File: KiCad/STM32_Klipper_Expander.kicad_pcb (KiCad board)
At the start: 2 copper layers, 48.3 x 48.3 mm, 44 parts, among them J1 USB_B_Micro, J10 Conn_01x01, J11 Conn_01x03, J12 Conn_01x02, J2 Conn_01x04, J3 Conn_02x05, J4 Conn_01x03, J5 Vin, J6 Screw_Terminal_01x08, J7 Conn_01x02, J8 Conn_01x02, J9 Conn_01x02, Q1 IRLML6344TRPBF, Q2 IRLML6344TRPBF, Q3 IRLML6344TRPBF, Q4 IRLML6344TRPBF, SW2 SW_SPST, U1 STM32F042F6Px, U2 AP2127K-3.3, U3 74LVC1G17

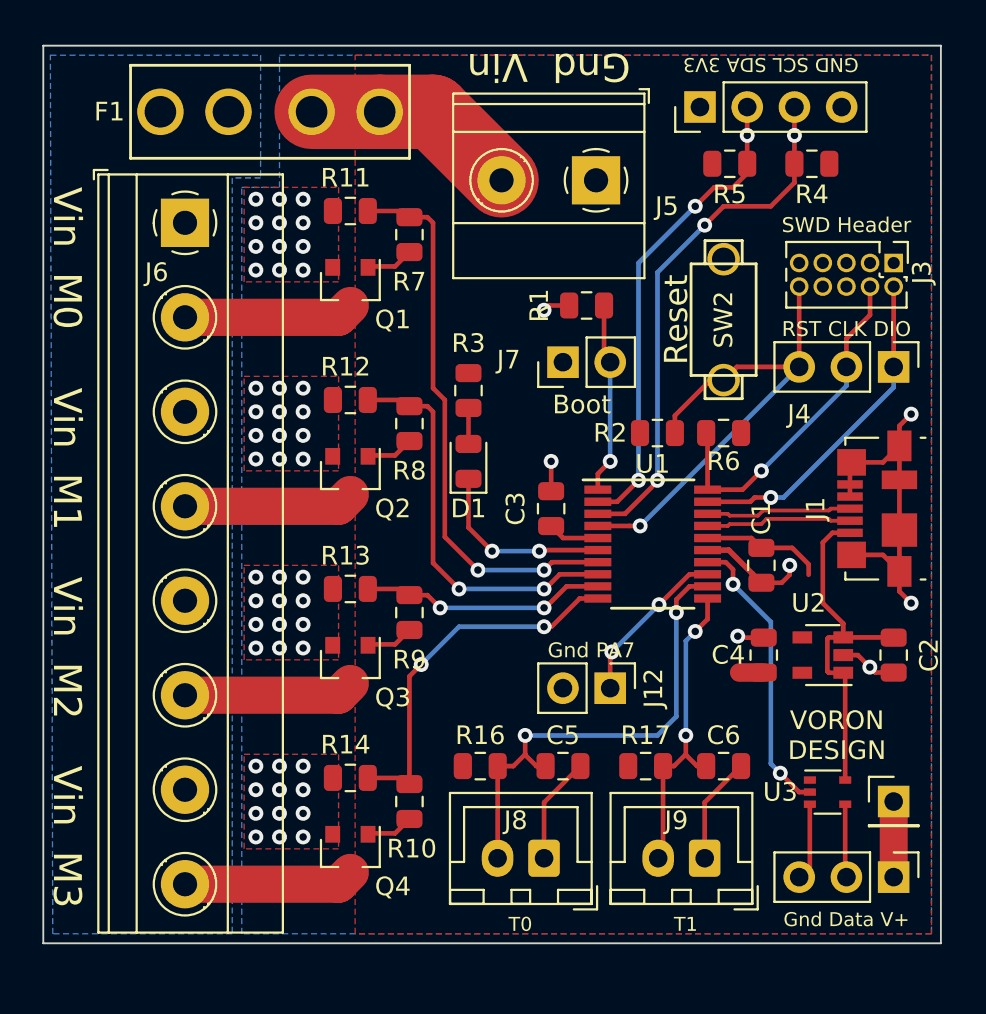
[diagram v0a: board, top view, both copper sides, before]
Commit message: Addition of mounting hole
APPARENTLY we need some way to mount this....
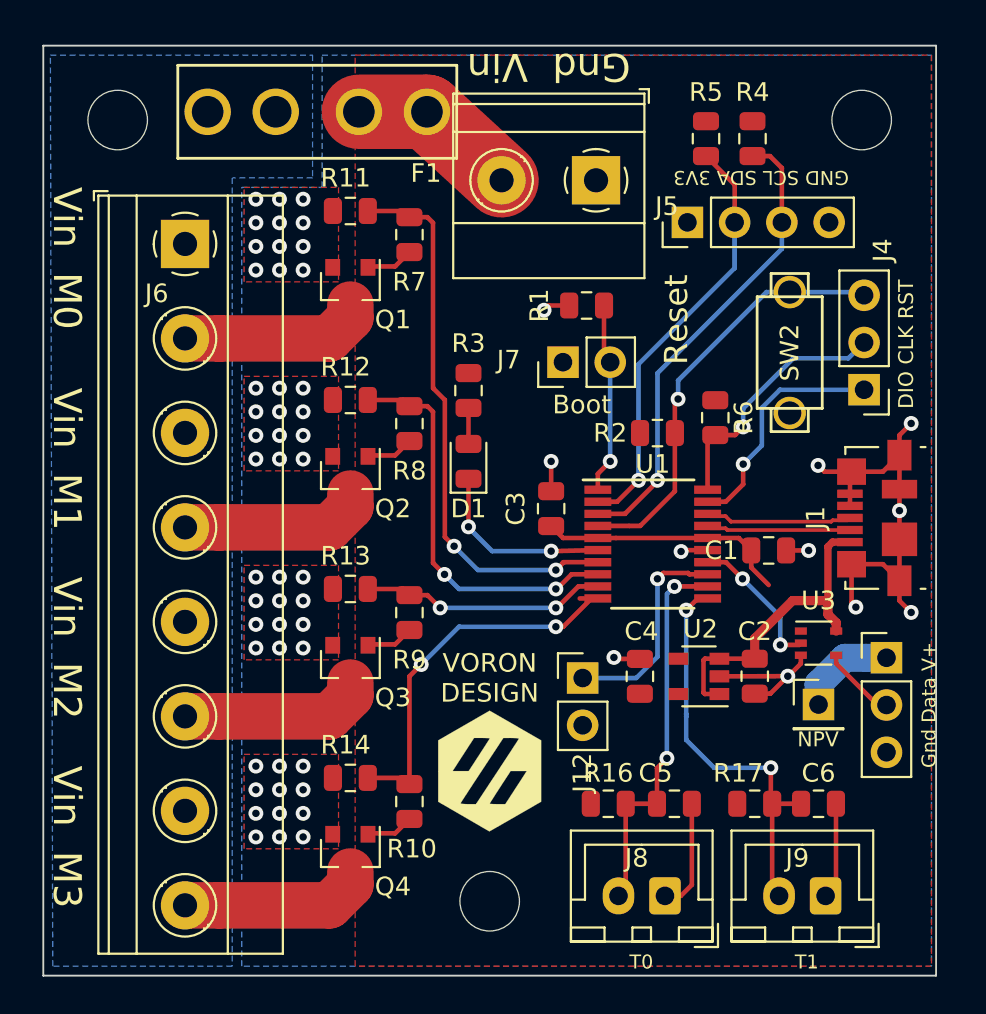
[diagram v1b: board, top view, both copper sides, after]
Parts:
- removed J3: Conn_02x05, Connector_PinHeader_1.27mm:PinHeader_2x05_P1.27mm_Vertical
- added G***: LOGO, TRA_KiCad_Footprints:VoronLogo_6pt5mm_silkScreen, F.Cu at (124.0, 90.7)
- added G***: LOGO, TRA_KiCad_Footprints:VoronLogo_6pt5mm_silkScreen, B.Cu at (124.0, 90.7)
- added H1: MountingHole, MountingHole:MountingHole_3.2mm_M3, F.Cu at (104.0, 55.7)
- added H2: MountingHole, MountingHole:MountingHole_3.2mm_M3, F.Cu at (124.0, 97.7)
- added H3: MountingHole, MountingHole:MountingHole_3.2mm_M3, F.Cu at (144.0, 55.7)
- moved J11 11.8 mm to (145.3, 84.7), turned to 0 degrees
- moved U3 8.02 mm to (141.7, 83.9)
- moved C2 7.56 mm to (138.2, 85.6)
- moved R16 7.17 mm to (130.4, 92.5)
- moved J8 6.81 mm to (133.4, 97.5)
- moved J9 6.81 mm to (142.1, 97.5)
- moved C4 6.76 mm to (132.1, 85.6)
- moved U2 6.76 mm to (135.3, 85.6)
- moved J10 6.60 mm to (141.7, 87.2)
- moved C5 6.32 mm to (133.9, 92.5)
- moved J2 6.23 mm to (134.6, 61.2)
- moved R17 6.20 mm to (138.2, 92.5)
- moved C6 5.49 mm to (141.7, 92.5)
- moved SW2 3.97 mm to (140.1, 68.2), turned to 270 degrees
- moved R4 3.47 mm to (138.1, 56.7), turned to 90 degrees
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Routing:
- net Neopixel: track 15.5 -> 7.79 mm
- net T1: track 16.8 -> 22.6 mm
- net T0: track 26.2 -> 20.6 mm
- net /SWDIO: track 18.0 -> 12.7 mm
- net /SWDCLK: track 18.2 -> 13.8 mm
- net /~RESET: track 27.4 -> 23.0 mm
- net /SCL: track 29.1 -> 25.4 mm, vias 3 -> 1
- net GPIO: track 8.35 -> 11.5 mm, vias 2 -> 1
- net +3V3: track 10.7 -> 13.6 mm
- net Net-(F1-Pad2): track 11.7 -> 9.11 mm
- net /SDA: track 25.2 -> 22.9 mm, vias 3 -> 1
- net VCC: track 19.3 -> 17.3 mm
- net Net-(J10-Pad1): track 4.06 -> 5.34 mm
- net /Mosfet1: track 9.15 -> 10.1 mm
- net /Mosfet0: track 9.15 -> 10.1 mm
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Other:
- board size 48.3 x 48.3 mm -> 48 x 50 mm
- board text added: "DIO CLK RST"
- board text added: "NPV"
- board text added: "PA7 Gnd"
- board text added: "RST PA14 PA13"
- board text removed: "Gnd PA7"
- board text removed: "PA13 PA14 RST"
- board text removed: "RST CLK DIO"
- board text removed: "SWD Header"
- board text removed: "Vin"

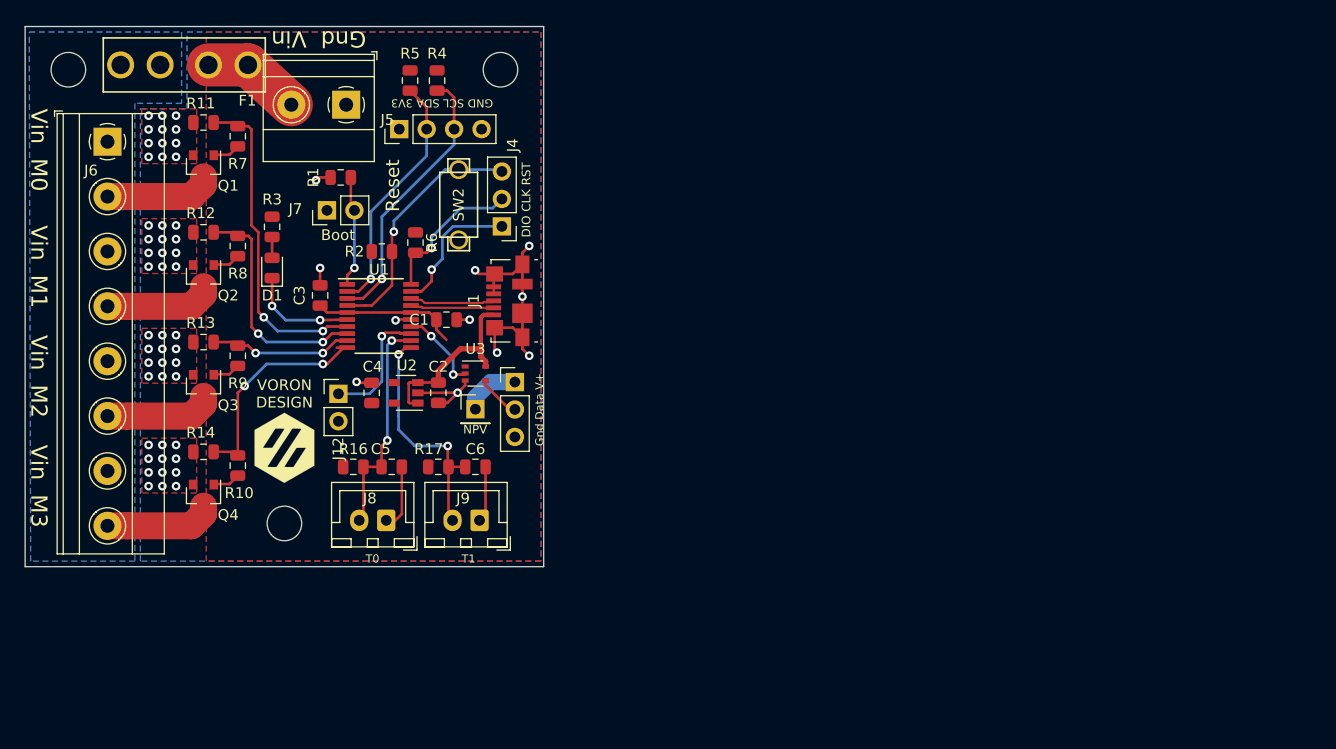
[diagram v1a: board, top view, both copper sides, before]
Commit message: Reorganization for more effiecent layout
Moving to a 100mm x 25mm PCB
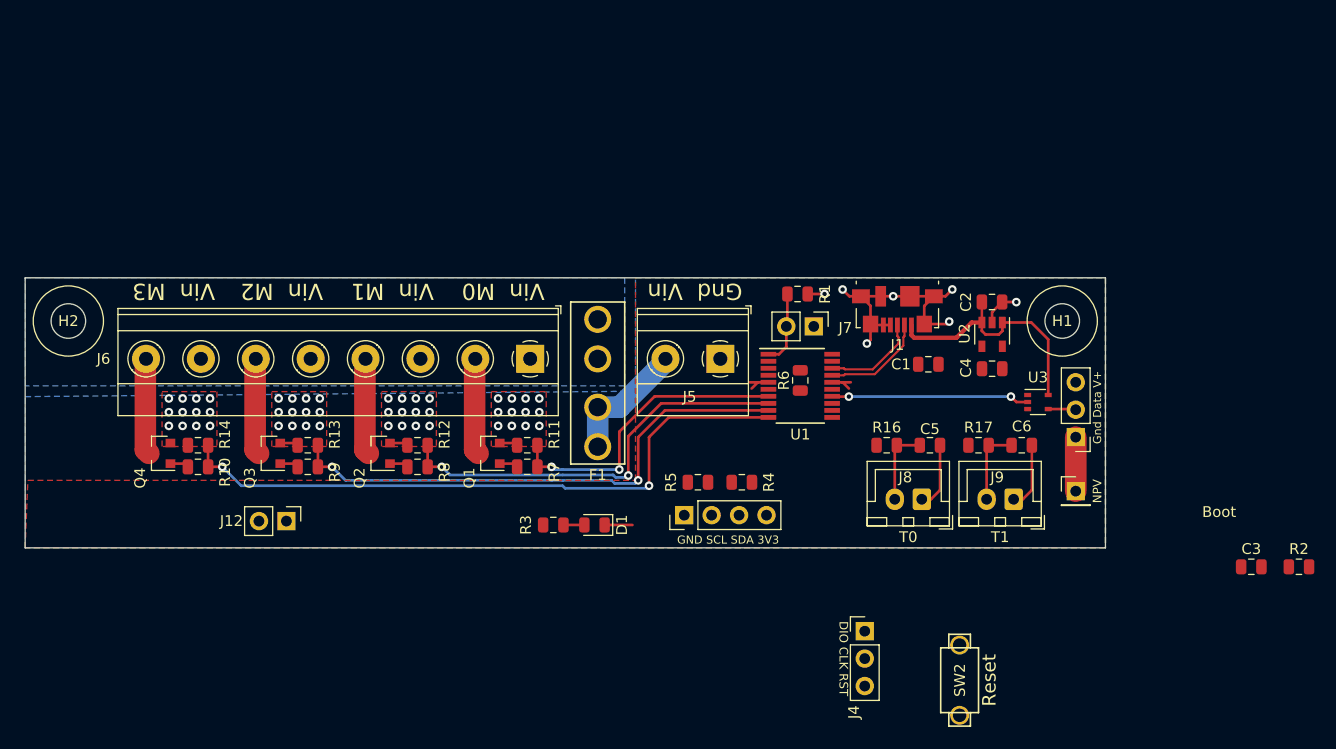
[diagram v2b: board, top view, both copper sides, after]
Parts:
- removed G*** (x2): LOGO, TRA_KiCad_Footprints:VoronLogo_6pt5mm_silkScreen
- removed H3: MountingHole, MountingHole:MountingHole_3.2mm_M3
- moved H1 94.9 mm to (196.0, 79.0)
- moved C3 89.8 mm to (213.5, 101.8), turned to 0 degrees
- moved R2 89.8 mm to (217.9, 101.8)
- moved SW2 63.9 mm to (186.5, 112.2), turned to 90 degrees
- moved C4 57.5 mm to (189.5, 83.4), turned to 0 degrees
- moved J10 56.1 mm to (197.2, 94.8)
- moved U2 54.5 mm to (189.5, 80.2), turned to 270 degrees
- moved J11 52.2 mm to (197.2, 89.8), turned to 180 degrees
- moved U3 52.1 mm to (193.8, 86.5)
- moved C2 51.9 mm to (189.5, 77.2), turned to 180 degrees
- moved C6 50.6 mm to (192.2, 90.5)
- moved J4 50.3 mm to (177.7, 107.7), turned to 0 degrees
- moved R17 50.0 mm to (188.2, 90.5)
- moved C5 49.9 mm to (183.8, 90.5)
- moved J8 49.6 mm to (183.0, 95.5)
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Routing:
- net PWM3: track 20.7 -> 60.0 mm
- net PWM2: track 13.3 -> 49.5 mm
- net /SCL: track 25.4 -> 0.00 mm, vias 1 -> 0
- net /~RESET: track 23.0 -> 0.00 mm, vias 1 -> 0
- net /SDA: track 22.9 -> 0.00 mm, vias 1 -> 0
- net PWM1: track 21.7 -> 38.9 mm
- net T1: track 22.6 -> 7.20 mm, vias 2 -> 0
- net /SWDCLK: track 13.8 -> 0.00 mm, vias 1 -> 0
- net T0: track 20.6 -> 7.20 mm, vias 2 -> 0
- net /SWDIO: track 12.7 -> 0.00 mm, vias 1 -> 0
- net GPIO: track 11.5 -> 0.00 mm, vias 1 -> 0
- net Neopixel: track 7.79 -> 18.3 mm
- net +3V3: track 13.6 -> 5.08 mm
- net /LED: track 10.2 -> 2.58 mm, vias 2 -> 0
- net VCC: track 17.3 -> 23.8 mm
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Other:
- board size 48 x 50 mm -> 100 x 25 mm
- board text removed: "VORON DESIGN"

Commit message: Routing and finalizations
Completed routing on the thinner variant. Need to gerenate BOM and CPL files for JLCPCB assembly
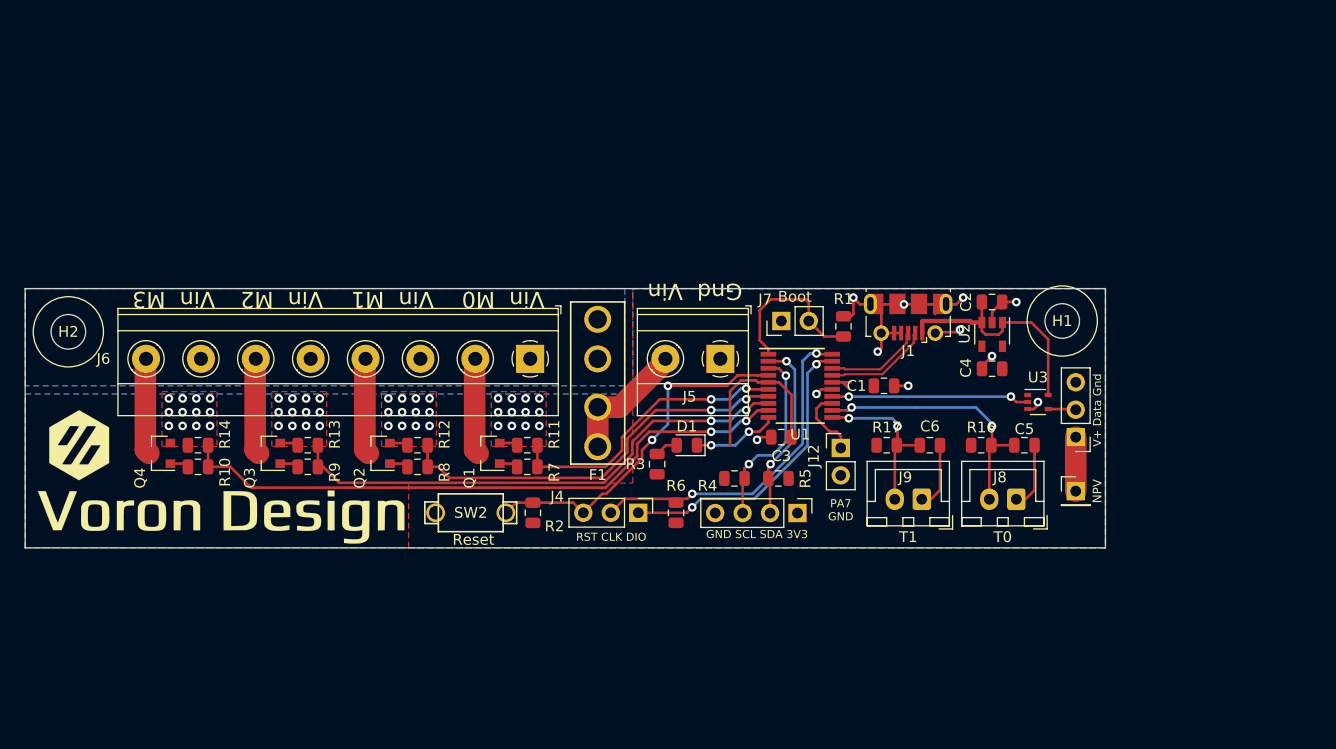
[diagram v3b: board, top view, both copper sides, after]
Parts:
- added G***: LOGO, TRA_KiCad_Footprints:VoronLogo_6pt5mm_silkScreen, F.Cu at (105.0, 90.5)
- added G***: LOGO, TRA_KiCad_Footprints:VoronDesign_Text_35x20, F.Cu at (118.2, 96.5)
- J1: footprint Connector_USB:USB_Micro-B_Molex_47346-0001 -> TRA_KiCad_Footprints:Molex-105017-0001-USBMicroB
- moved R2 71.1 mm to (147.0, 96.8), turned to 90 degrees
- moved J12 51.8 mm to (175.5, 90.8), turned to 0 degrees
- moved SW2 47.8 mm to (141.2, 96.8), turned to 180 degrees
- moved C3 45.1 mm to (170.0, 89.8)
- moved J4 23.7 mm to (156.8, 96.8), turned to 270 degrees
- moved R6 16.8 mm to (160.2, 96.8)
- moved D1 11.3 mm to (161.2, 90.5)
- moved R3 11.1 mm to (158.5, 92.2), turned to 270 degrees
- moved J2 10.5 mm to (171.5, 96.8), turned to 270 degrees
- moved C5 8.75 mm to (192.5, 90.5)
- moved J8 8.75 mm to (191.8, 95.5)
- moved R16 8.75 mm to (188.5, 90.5)
- moved C6 8.50 mm to (183.8, 90.5)
- moved J9 8.50 mm to (183.0, 95.5)
- moved R17 8.50 mm to (179.8, 90.5)
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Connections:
- U1 pad 10: PWM3 -> /LED
- U1 pad 6: /LED -> PWM0
- U1 pad 7: PWM0 -> PWM1
- U1 pad 8: PWM1 -> PWM2
- U1 pad 9: PWM2 -> PWM3
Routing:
- net /~RESET: track 0.00 -> 32.9 mm, vias 0 -> 2
- net /SWDCLK: track 0.00 -> 31.1 mm, vias 0 -> 2
- net /SWDIO: track 0.00 -> 27.7 mm, vias 0 -> 2
- net T0: track 7.20 -> 24.8 mm, vias 0 -> 2
- net /SDA: track 0.00 -> 17.3 mm, vias 0 -> 2
- net /SCL: track 0.00 -> 17.0 mm, vias 0 -> 2
- net +3V3: track 5.08 -> 18.1 mm
- net T1: track 7.20 -> 15.5 mm, vias 0 -> 2
- net /BOOT0: track 6.88 -> 15.0 mm
- net GPIO: track 0.00 -> 6.59 mm
- net GND: track 45.7 -> 52.3 mm, vias 55 -> 59
- net /LED: track 2.58 -> 7.96 mm, vias 0 -> 2
- net PWM3: track 60.0 -> 58.3 mm
- net VCC: track 23.8 -> 22.3 mm
- net PWM2: track 49.5 -> 48.0 mm
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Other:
- board size 100 x 25 mm -> 100 x 24 mm
- board text added: "Gnd PB1 V+"
- board text added: "Klipper Expansion Board Timothy Abraham"
- board text added: "PA13 PA14 RST"
- board text added: "PA7 GND"
- board text added: "RST CLK DIO"
- board text added: "V+ Data Gnd"
- board text removed: "DIO CLK RST"
- board text removed: "Gnd Data V+"
- board text removed: "RST PA14 PA13"
- board text removed: "Vin PB1 Gnd"

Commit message: for real this time
ACTUALLY pushing the changes and not just some gerber updates...
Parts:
- moved J10 1.75 mm to (197.2, 96.5)
- moved J11 1.75 mm to (197.2, 91.5)
- moved H1 1.00 mm to (196.0, 80.0)
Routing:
- net Net-(J11-Pad2): track 2.57 -> 3.85 mm
- net VCC: track 22.3 -> 21.5 mm
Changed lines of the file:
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@@
     (thickness 1.6)
     (drawings 35)
-    (tracks 360)
+    (tracks 362)
     (zones 0)
     (modules 47)
@@
   )
   (module Connector_PinHeader_2.54mm:PinHeader_1x01_P2.54mm_Vertical (layer F.Cu)
-    (at 197.25 94.75)
+    (at 197.25 96.5)
     (descr "Through hole straight pin header, 1x01, 2.54mm pitch, single row")
     (tags "Through hole pin header THT 1x01 2.54mm single row")
@@
   )
   (module MountingHole:MountingHole_3.2mm_M3 (layer F.Cu)
-    (at 196 79)
+    (at 196 80)
     (descr "Mounting Hole 3.2mm, no annular, M3")
     (tags "mounting hole 3.2mm no annular m3")
@@
   )
   (module Connector_PinHeader_2.54mm:PinHeader_1x03_P2.54mm_Vertical (layer F.Cu)
-    (at 197.25 89.75 180)
+    (at 197.25 91.5 180)
     (descr "Through hole straight pin header, 1x03, 2.54mm pitch, single row")
     (tags "Through hole pin header THT 1x03 2.54mm single row")
@@
   )
   (gr_circle (center 104 80) (end 107.25 80) (layer F.SilkS) (width 0.12))
-  (gr_circle (center 196 79) (end 199.25 79) (layer F.SilkS) (width 0.12))
+  (gr_circle (center 196 80) (end 199.25 80) (layer F.SilkS) (width 0.12))
   (gr_text T1 (at 181.75 99) (layer F.SilkS)
     (effects (font (size 1 1) (thickness 0.15)))
@@
     (effects (font (size 0.75 0.75) (thickness 0.1)) (justify mirror))
   )
-  (gr_text "NPV\n" (at 199.25 94.75 90) (layer F.SilkS)
+  (gr_text "NPV\n" (at 199.25 96.5 90) (layer F.SilkS)
     (effects (font (size 0.8 0.8) (thickness 0.15)))
   )
-  (gr_text "V+ Data Gnd" (at 199.25 87.25 90) (layer F.SilkS)
+  (gr_text "V+ Data Gnd" (at 199.25 89 90) (layer F.SilkS)
     (effects (font (size 0.75 0.75) (thickness 0.1)))
   )
@@
     (effects (font (size 0.75 0.75) (thickness 0.1)))
   )
-  (gr_text "Gnd PB1 V+\n" (at 199.25 87.25 90) (layer B.SilkS)
+  (gr_text "Gnd PB1 V+\n" (at 199.25 89 90) (layer B.SilkS)
     (effects (font (size 0.75 0.75) (thickness 0.1)) (justify mirror))
   )
@@
   (segment (start 188.559 77.2445) (end 188.5635 77.24) (width 0.25) (layer F.Cu) (net 31))
   (segment (start 188.559 79.139) (end 188.559 77.2445) (width 0.25) (layer F.Cu) (net 31))
-  (segment (start 194.7 85.85) (end 194.7 80.7) (width 0.25) (layer F.Cu) (net 31))
-  (segment (start 193.139 79.139) (end 190.459 79.139) (width 0.25) (layer F.Cu) (net 31))
-  (segment (start 194.7 80.7) (end 193.139 79.139) (width 0.25) (layer F.Cu) (net 31))
   (segment (start 187.611 79.139) (end 188.559 79.139) (width 0.4) (layer F.Cu) (net 31))
   (segment (start 183.042 79.0465) (end 183.042 80.1215) (width 0.4) (layer F.Cu) (net 31))
@@
   (segment (start 187.468499 78.996499) (end 183.092001 78.996499) (width 0.4) (layer F.Cu) (net 31))
   (segment (start 187.611 79.139) (end 187.468499 78.996499) (width 0.4) (layer F.Cu) (net 31))
-  (segment (start 197.25 94.75) (end 197.25 89.75) (width 2) (layer F.Cu) (net 32))
-  (segment (start 197.19 87.15) (end 197.25 87.21) (width 0.25) (layer F.Cu) (net 33))
-  (segment (start 194.7 87.15) (end 197.19 87.15) (width 0.25) (layer F.Cu) (net 33))
+  (segment (start 194.7 85.85) (end 194.7 82.2) (width 0.25) (layer F.Cu) (net 31))
+  (segment (start 191.639 79.139) (end 190.459 79.139) (width 0.25) (layer F.Cu) (net 31))
+  (segment (start 194.7 82.2) (end 191.639 79.139) (width 0.25) (layer F.Cu) (net 31))
+  (segment (start 197.25 96.5) (end 197.25 91.5) (width 2) (layer F.Cu) (net 32))
+  (segment (start 197.19 88.9) (end 197.25 88.96) (width 0.25) (layer F.Cu) (net 33))
+  (segment (start 194.7 87.15) (end 194.7 87.95) (width 0.25) (layer F.Cu) (net 33))
+  (segment (start 195.71 88.96) (end 197.25 88.96) (width 0.25) (layer F.Cu) (net 33))
+  (segment (start 194.7 87.95) (end 195.71 88.96) (width 0.25) (layer F.Cu) (net 33))
   (zone (net 2) (net_name GND) (layer F.Cu) (hatch edge 0.508)
     (connect_pads (clearance 0.508))

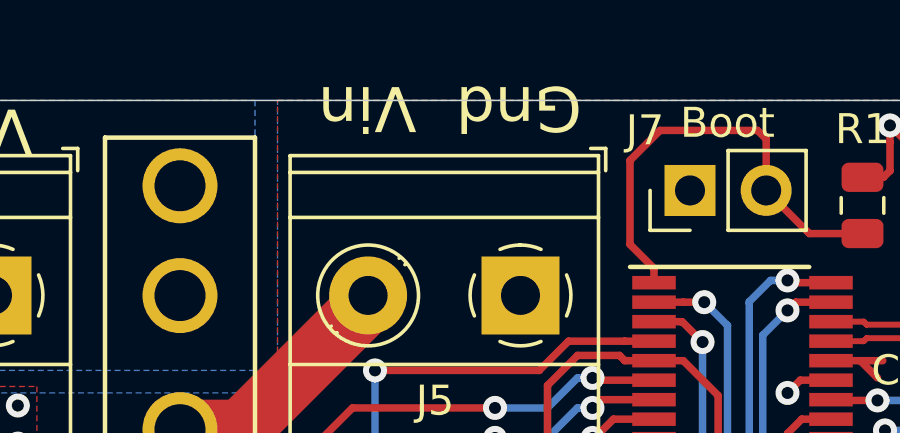
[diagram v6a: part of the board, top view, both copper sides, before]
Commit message: Silkscreen changes
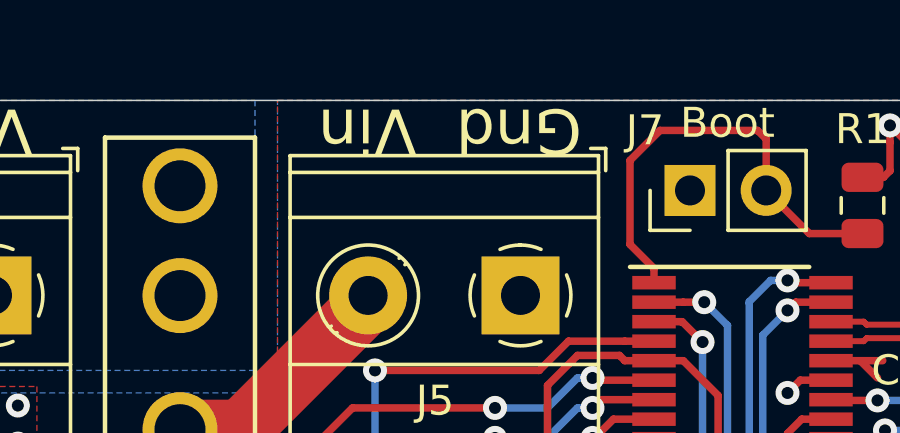
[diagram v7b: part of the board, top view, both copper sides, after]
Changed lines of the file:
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@@
     (effects (font (size 1.5 1.5) (thickness 0.2)))
   )
-  (gr_text "Gnd  Vin" (at 162 76.25 180) (layer F.SilkS)
+  (gr_text "Gnd  Vin" (at 162 77 180) (layer F.SilkS)
     (effects (font (size 1.5 1.5) (thickness 0.2)))
   )
